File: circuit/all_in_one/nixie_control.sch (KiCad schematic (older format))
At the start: 21 parts, among them IC1 ATMEGA328P-A, P2 CONN_02X04, Q3 Q_NPN_EBC, Q4 Q_NPN_EBC, SW1 SW_PUSH, SW2 SW_PUSH, U3 TLP521, U4 TLP521, U5 HEF4028, U6 K155ID1, U7 TLP521, U8 TLP521, Y1 16MHZ

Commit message: Finished select all the component footprint
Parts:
- SW1, SW2: footprint (none) -> Buttons_Switches_ThroughHole:SW_PUSH-12mm
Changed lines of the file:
@@
 F 0 "SW2" H 8950 4960 50  0000 C CNN
 F 1 "SW_PUSH" H 8800 4770 50  0000 C CNN
-F 2 "" H 8800 4850 60  0001 C CNN
+F 2 "Buttons_Switches_ThroughHole:SW_PUSH-12mm" H 8800 4850 60  0001 C CNN
 F 3 "" H 8800 4850 60  0000 C CNN
 	1    8800 4850
@@
 F 0 "SW1" H 5850 6110 50  0000 C CNN
 F 1 "SW_PUSH" H 5700 5920 50  0000 C CNN
-F 2 "" H 5700 6000 60  0001 C CNN
+F 2 "Buttons_Switches_ThroughHole:SW_PUSH-12mm" H 5700 6000 60  0001 C CNN
 F 3 "" H 5700 6000 60  0000 C CNN
 	1    5700 6000

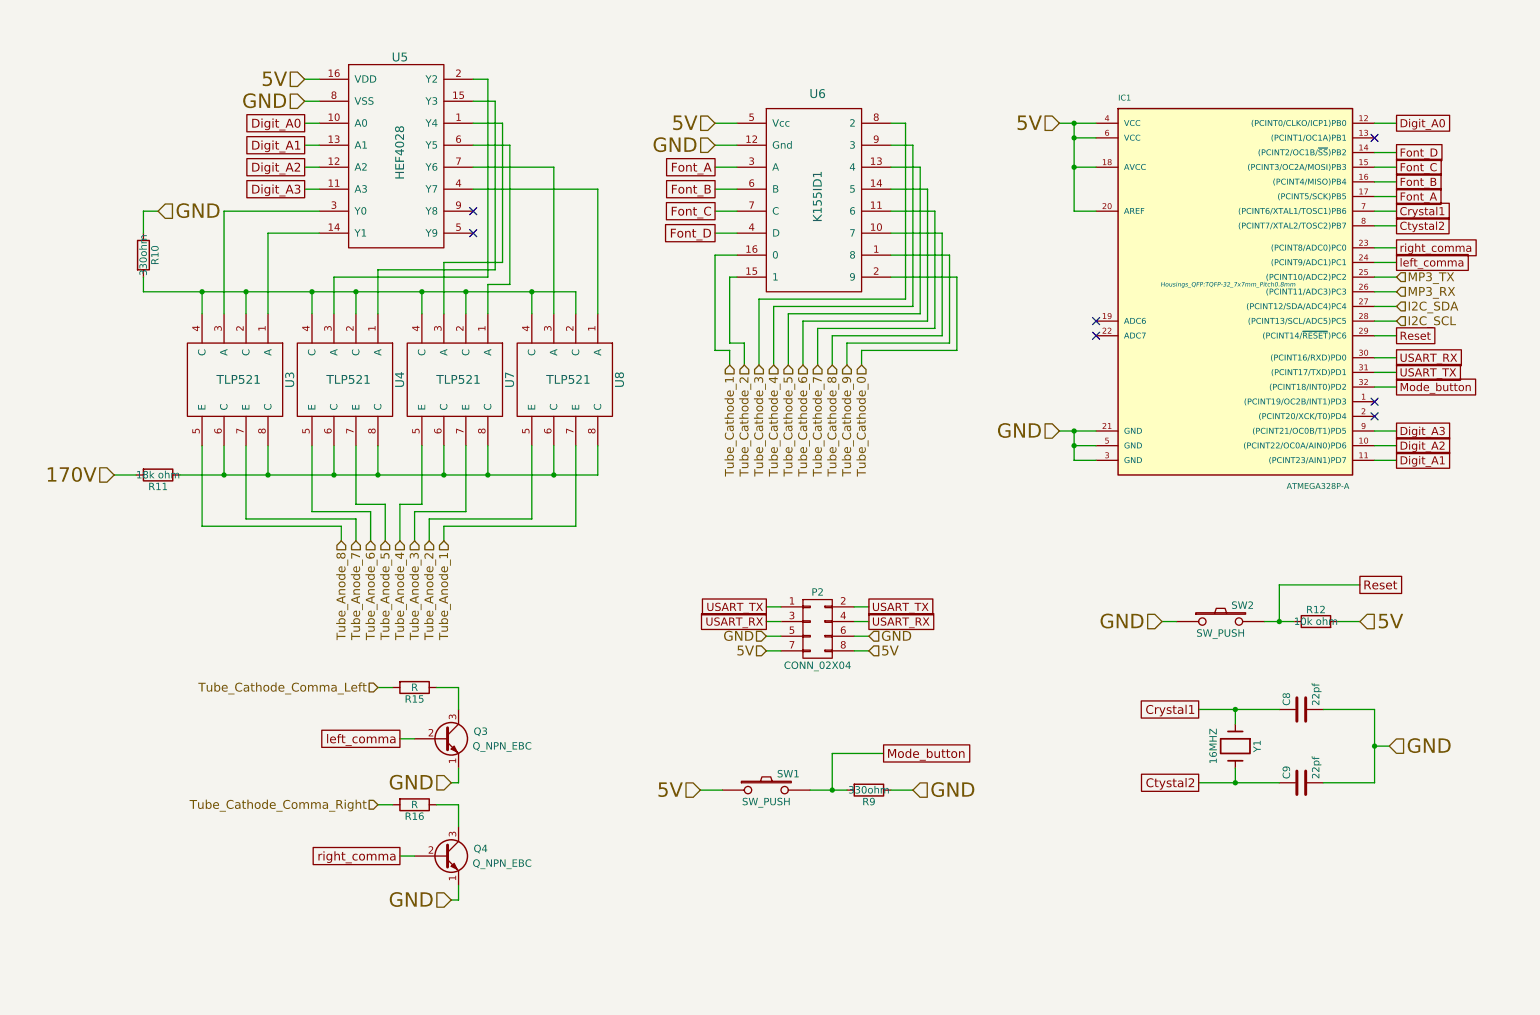
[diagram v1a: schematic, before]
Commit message: Finsihed placing all the components
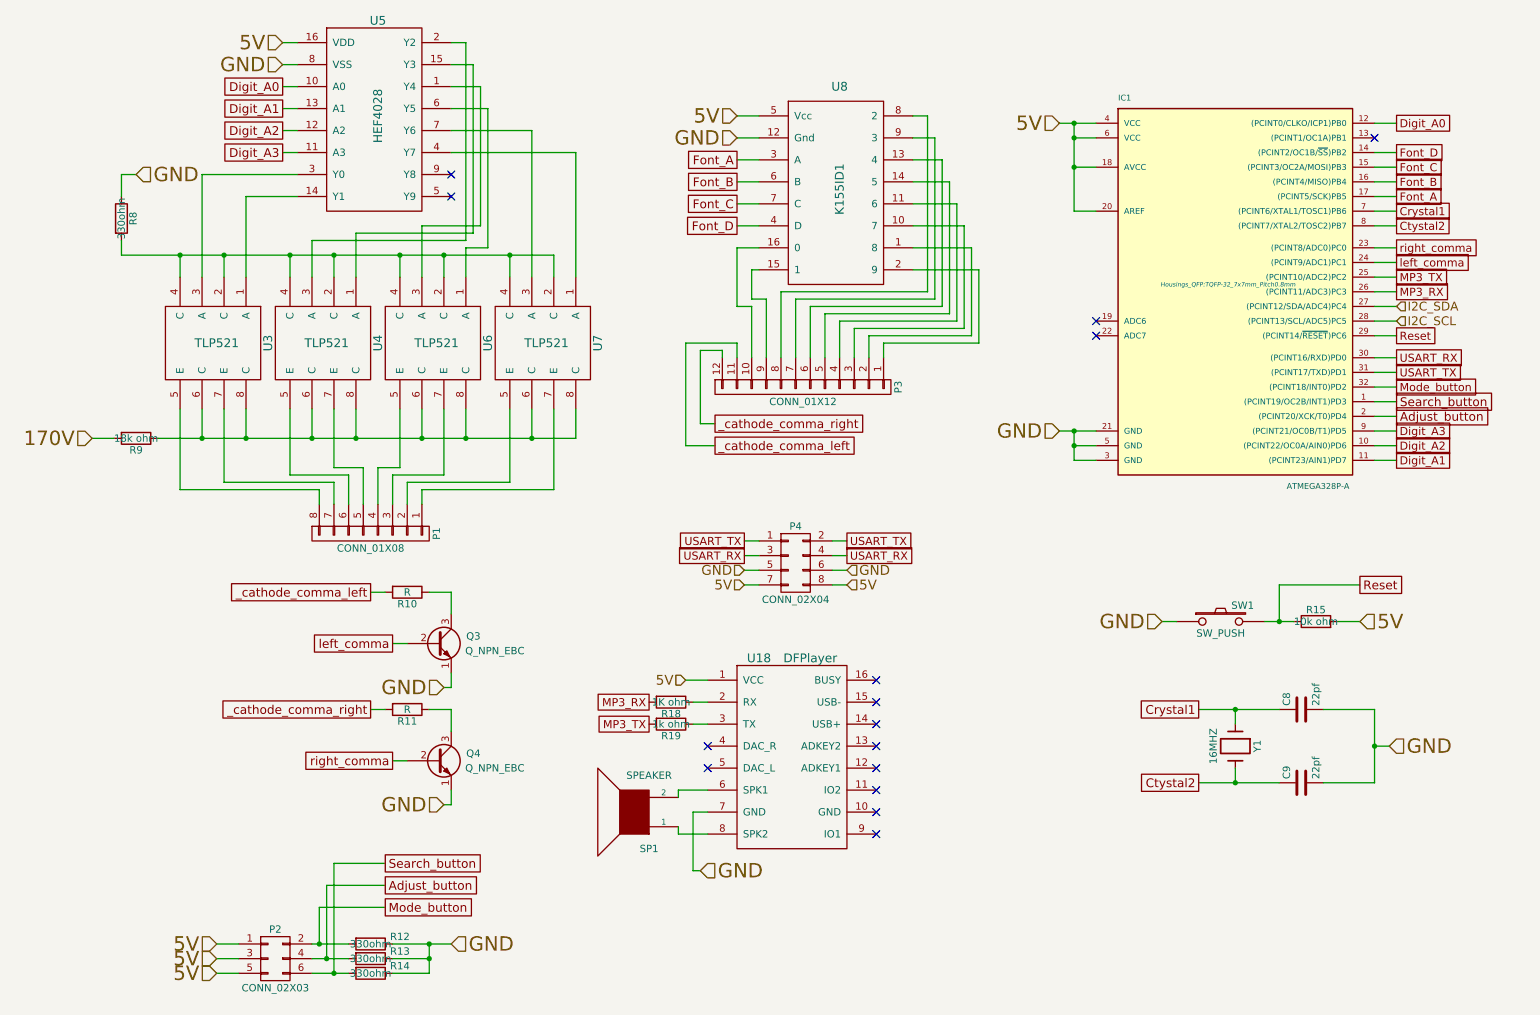
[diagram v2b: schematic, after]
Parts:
- removed SW1: SW_PUSH, Buttons_Switches_ThroughHole:SW_PUSH-12mm, symbol SW_PUSH
- added P1: CONN_01X08, Pin_Headers:Pin_Header_Straight_1x08, symbol CONN_01X08
- added P2: CONN_02X03, Pin_Headers:Pin_Header_Straight_2x03, symbol CONN_02X03
- added P3: CONN_01X12, Pin_Headers:Pin_Header_Straight_1x12, symbol CONN_01X12
- added R13, R14: 330ohm, Resistors_SMD:R_0805_HandSoldering, symbol R
- added R18: 1K ohm, Resistors_SMD:R_0805_HandSoldering, symbol R
- added R19: 1k ohm, Resistors_SMD:R_0805_HandSoldering, symbol R
- added SP1: SPEAKER, Connect:PINHEAD1-2, symbol SPEAKER
- added U18: DFPlayer, dfplayer:DFPlayer, symbol DFPlayer
- P4: renamed from P2; footprint Socket_Strips:Socket_Strip_Straight_2x04 -> Pin_Headers:Pin_Header_Straight_2x04
- Q3, Q4: footprint Housings_TO-92:TO-92_Inline_Narrow_Oval -> TO_SOT_Packages_THT:TO-92_Inline_Narrow_Oval
- SW1: renamed from SW2; footprint Buttons_Switches_ThroughHole:SW_PUSH-12mm -> Buttons_Switches_SMD:SW_SPST_PTS645
- renumbered R15 to R10, R16 to R11, R9 to R12, R12 to R15, R10 to R8, R11 to R9, U7 to U6, U8 to U7, U6 to U8
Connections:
- net 5V: now also P2.1 (P1), P2.3 (P3), P2.5 (P5), U18.1 (VCC)
- net GND: now also R13.1, R14.1, U18.7 (GND)
- net MP3_RX: now also R18.2
- net MP3_TX: now also R19.2
- net Mode_button: now also P2.2 (P2)
- net Search_button: now reaches IC1.1 ((PCINT19/OC2B/INT1)PD3)
- net Search_button: now also P2.6 (P6), R14.2
- net Adjust_button: now reaches IC1.2 ((PCINT20/XCK/T0)PD4)
- net Adjust_button: now also P2.4 (P4), R13.2
- net Tube_Anode_1: no longer names the net of U7.7 (E)
- net Tube_Anode_1: now also P1.1 (P1)
- net Tube_Anode_2: no longer names the net of U7.5 (E)
- net Tube_Anode_2: now also P1.2 (P2)
- net Tube_Anode_3: no longer names the net of U6.7 (E)
- net Tube_Anode_3: now also P1.3 (P3)
- net Tube_Anode_4: no longer names the net of U6.5 (E)
- net Tube_Anode_4: now also P1.4 (P4)
- net Tube_Anode_5: no longer names the net of U4.7 (E)
- net Tube_Anode_5: now also P1.5 (P5)
- net Tube_Anode_6: no longer names the net of U4.5 (E)
- net Tube_Anode_6: now also P1.6 (P6)
- net Tube_Anode_7: no longer names the net of U3.7 (E)
- net Tube_Anode_7: now also P1.7 (P7)
- net Tube_Anode_8: no longer names the net of U3.5 (E)
- net Tube_Anode_8: now also P1.8 (P8)
- net Tube_Cathode_0: no longer names the net of U8.2 (9)
- net Tube_Cathode_0: now also P3.1 (P1)
- net Tube_Cathode_1: no longer names the net of U8.16 (0)
- net Tube_Cathode_1: now also P3.10 (P10)
- net Tube_Cathode_2: no longer names the net of U8.15 (1)
- net Tube_Cathode_2: now also P3.9 (P9)
- net Tube_Cathode_3: no longer names the net of U8.8 (2)
- net Tube_Cathode_3: now also P3.8 (P8)
- net Tube_Cathode_4: no longer names the net of U8.9 (3)
- net Tube_Cathode_4: now also P3.7 (P7)
- net Tube_Cathode_5: no longer names the net of U8.13 (4)
- net Tube_Cathode_5: now also P3.6 (P6)
- net Tube_Cathode_6: no longer names the net of U8.14 (5)
- net Tube_Cathode_6: now also P3.5 (P5)
- net Tube_Cathode_7: no longer names the net of U8.11 (6)
- net Tube_Cathode_7: now also P3.4 (P4)
- net Tube_Cathode_8: no longer names the net of U8.10 (7)
- net Tube_Cathode_8: now also P3.3 (P3)
- net Tube_Cathode_9: no longer names the net of U8.1 (8)
- net Tube_Cathode_9: now also P3.2 (P2)
- net Tube_Cathode_Comma_Left renamed _cathode_comma_left
- net _cathode_comma_left: now also P3.11 (P11)
- net Tube_Cathode_Comma_Right renamed _cathode_comma_right
- net _cathode_comma_right: now also P3.12 (P12)
- new net: R18.1, U18.2 (RX)
- new net: R19.1, U18.3 (TX)
- new net: SP1.2, U18.6 (SPK1)
- new net: SP1.1, U18.8 (SPK2)
- no-connect marks 7 -> 15
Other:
- moved on the sheet: P4, Q3, Q4, R10, R11, R12, R8, R9, U3, U4, U5, U6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

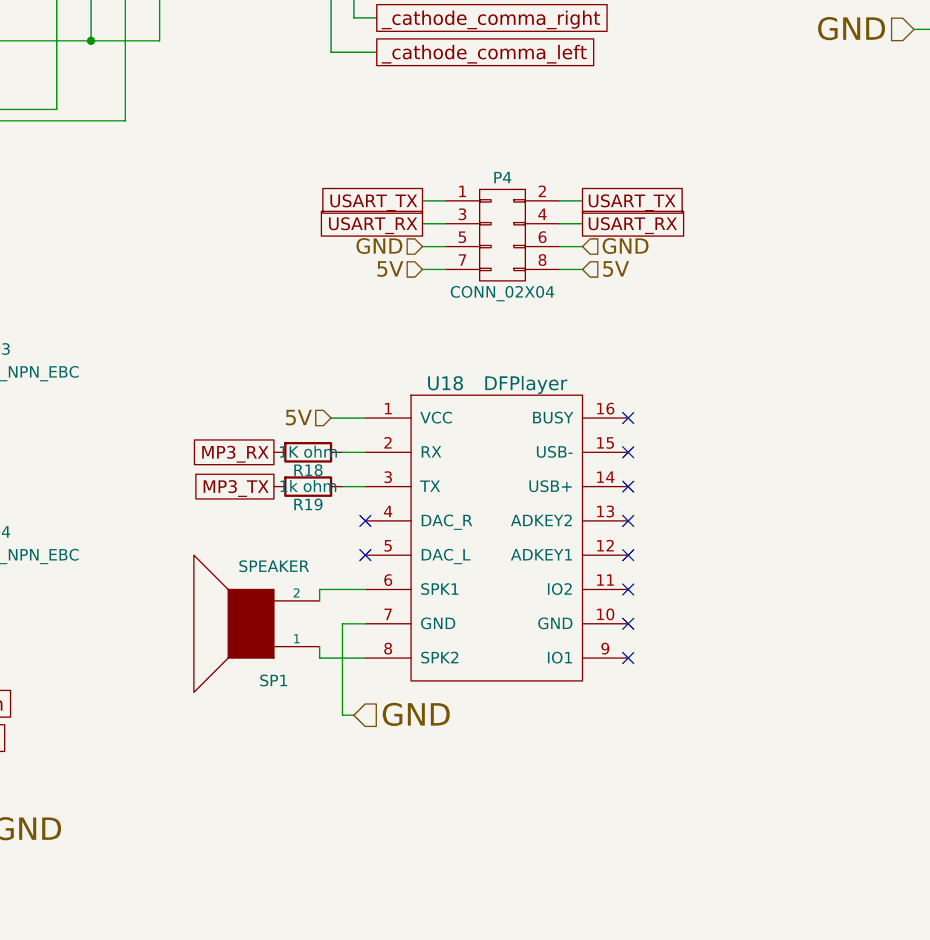
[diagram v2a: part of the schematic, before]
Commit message: New hardware is almost finished
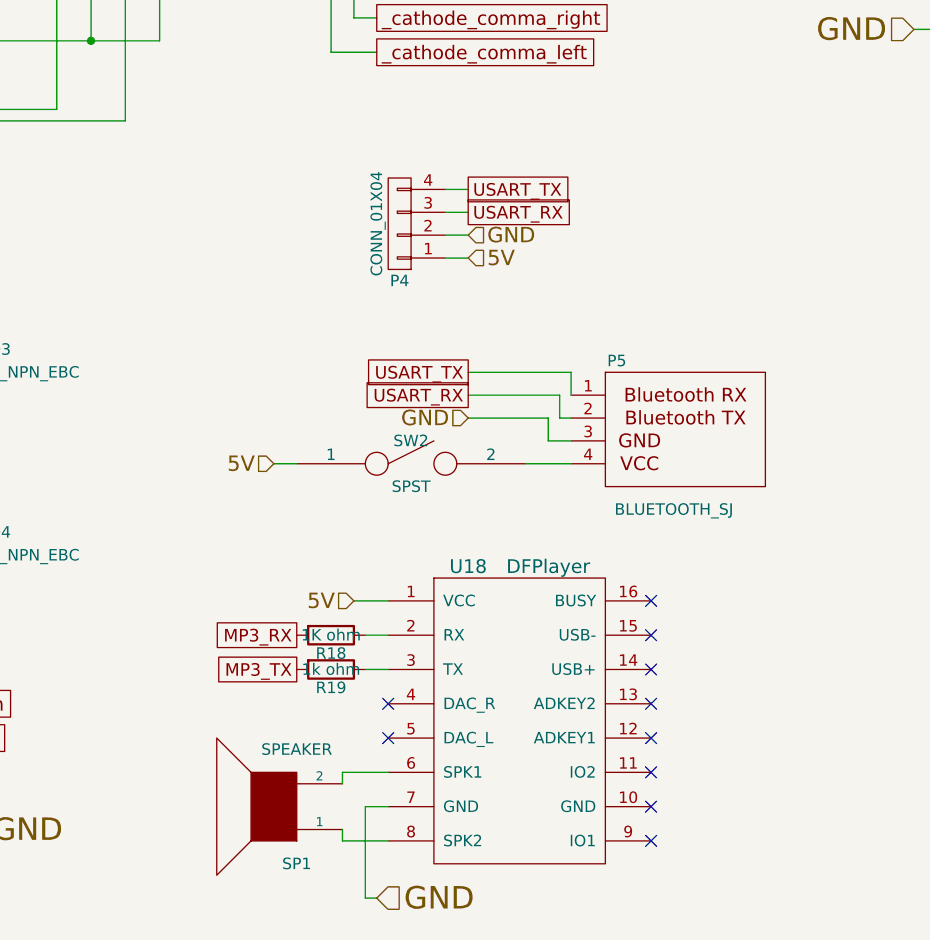
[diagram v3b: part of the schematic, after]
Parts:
- removed P4: CONN_02X04, Pin_Headers:Pin_Header_Straight_2x04, symbol CONN_02X04
- added P4: CONN_01X04, Pin_Headers:Pin_Header_Angled_1x04, symbol CONN_01X04
- added P5: BLUETOOTH_SJ, HC06:HC06, symbol BLUETOOTH_SJ
- added SW2: SPST, Pin_Headers:Pin_Header_Straight_1x02, symbol SPST
- P1: footprint Pin_Headers:Pin_Header_Straight_1x08 -> SMD_PIN_2_BY_4_REVERSE:SMD_PIN_2_BY_4_REVERSE
- P2: footprint Pin_Headers:Pin_Header_Straight_2x03 -> SMD_PIN_2_BY_3_REVERSE:SMD_PIN_2_BY_3_REVERSE
- P3: footprint Pin_Headers:Pin_Header_Straight_1x12 -> SMD_PIN_2_BY_6_REVERSE:SMD_PIN_2_BY_6_REVERSE
- R10, R11, R12, R13, R14, R15, R18, R19, R8, R9: footprint Resistors_SMD:R_0805_HandSoldering -> Resistors_SMD:R_1206_HandSoldering
- U3, U4, U6, U7: footprint SMD_Packages:DIP-8_SMD -> Housings_DIP:DIP-8_W7.62mm
- U5: footprint SMD_Packages:SO-16-N -> Housings_DIP:DIP-16_W7.62mm
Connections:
- net 5V: now also P4.1 (P1), SW2.1
- net GND: now also P4.2 (P2), P5.3 (P3)
- net USART_RX: now also P4.3 (P3), P5.2 (P2)
- net USART_TX: now also P4.4 (P4), P5.1 (BLUETOOTH_RX)
- new net: P5.4 (P4), SW2.2
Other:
- moved on the sheet: R18, R19, SP1, U18
